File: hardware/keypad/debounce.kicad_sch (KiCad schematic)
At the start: 108 parts, among them SW401 DISPLAY, SW402 RUN, SW403 LEFT, SW404 MEMORY, SW405 COMP, SW406 UP, SW407 MENU, SW408 DOWN, SW409 INFEED, SW410 ENTER, SW411 RIGHT, SW412 DECIMAL, SW413 HEAD_POS, SW414 1, SW415 4, SW416 7, SW417 FTI, SW418 2, SW419 5, SW420 8, SW421 SHEAR, SW422 3, SW423 6, SW424 9, SW425 PAUSE, SW426 PLUS, SW427 MINUS, SW428 0, U401 SN74HC14PWR, U402 SN74HC14PWR, U403 SN74HC14PWR, U404 SN74HC14PWR, U405 SN74HC14PWR, U406 SN74LVC2G14DBV, U407 PCF8575DBR, U408 PCF8575DBR, U409 74LVC1G32GW,125

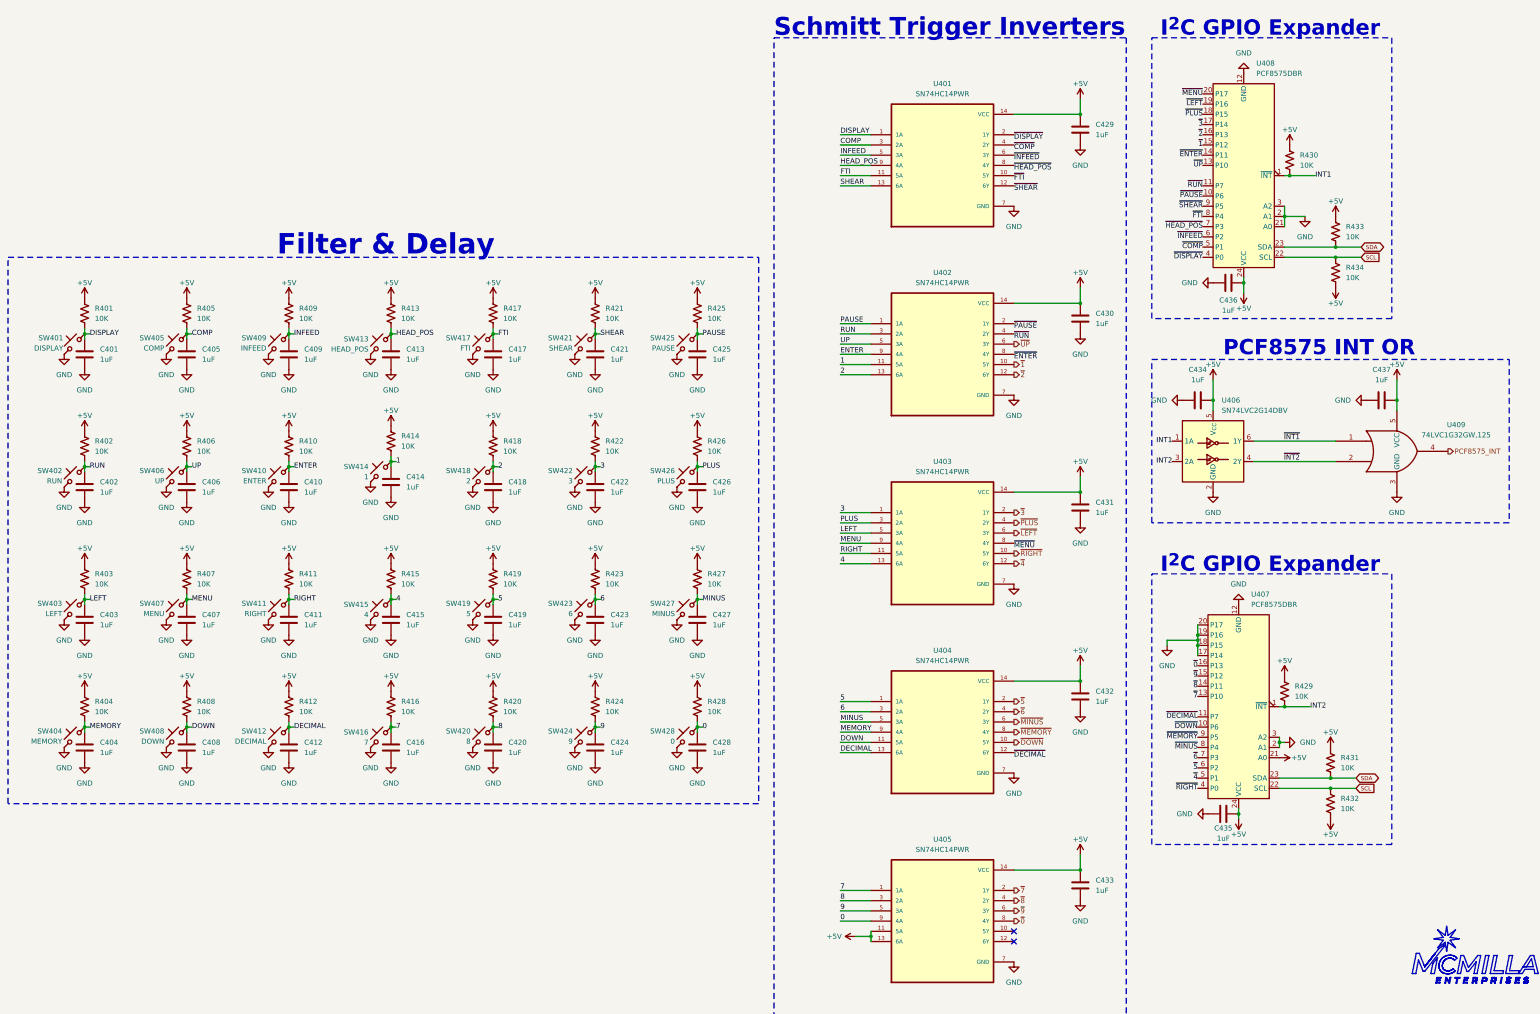
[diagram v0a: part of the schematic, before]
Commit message: [fix] repeater and sbc shutdown circuit
Fixed repeater and SBC shutdown circuit. Switched +5V VCC to +3.3V. Added C211
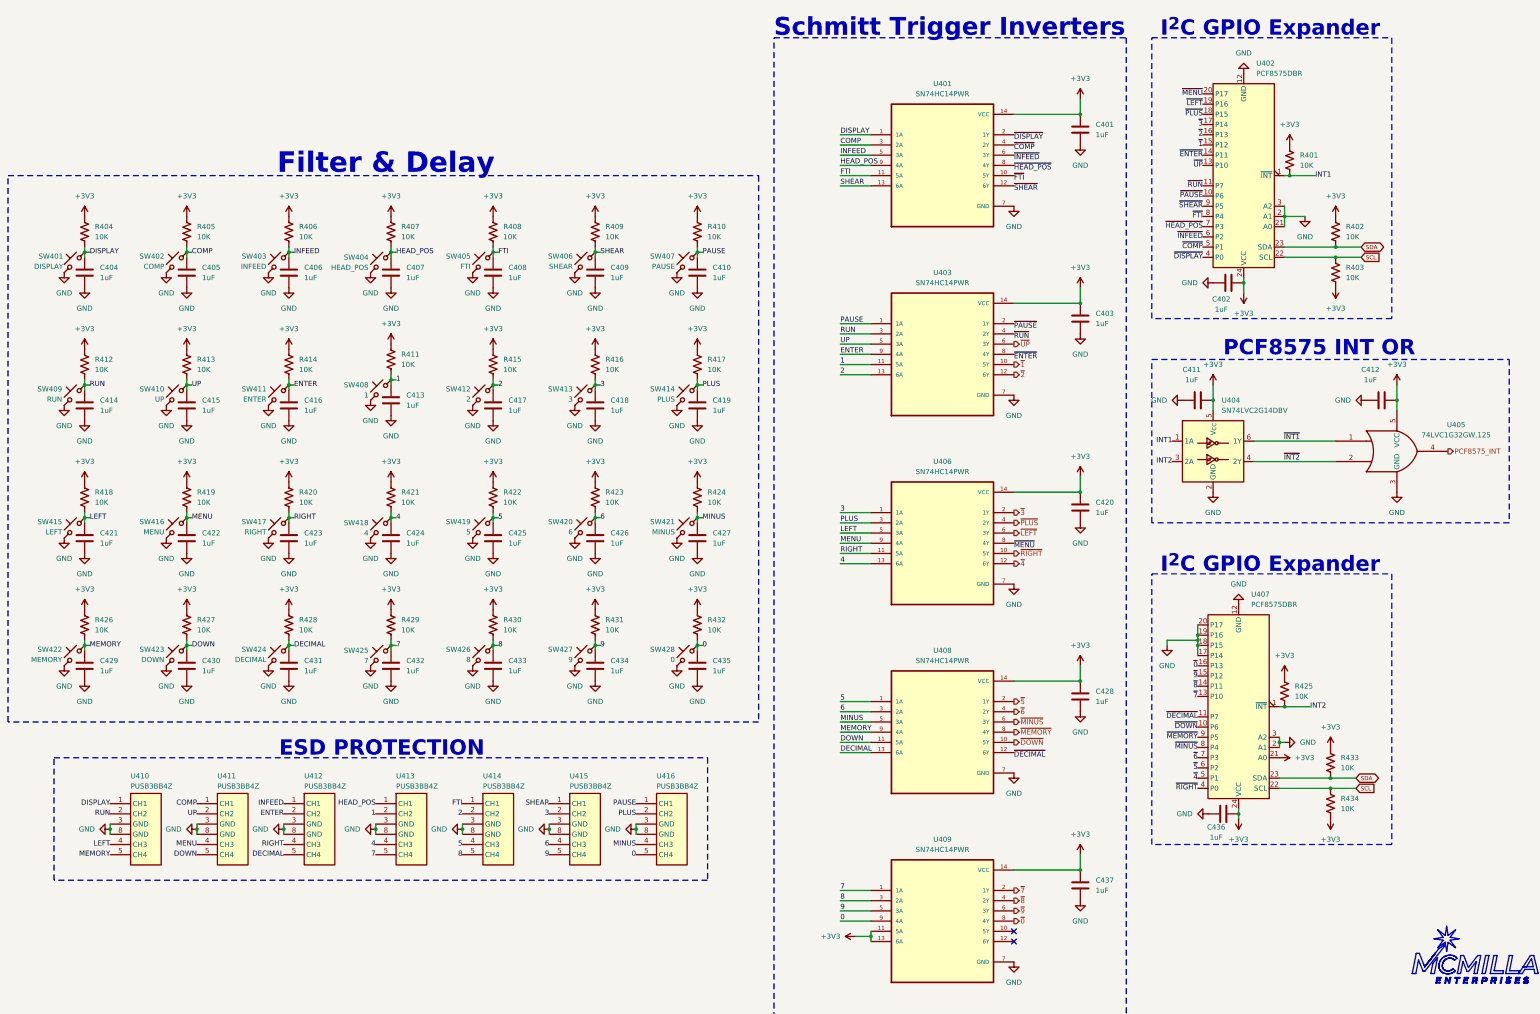
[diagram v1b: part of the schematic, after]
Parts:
- added U410, U411, U412, U413, U414, U415, U416: PUSB3BB4Z, PUSB3BB4Z:SON50P100X250X50-10N, symbol PUSB3BB4Z:PUSB3BB4Z
- renumbered C429 to C401, C436 to C402, C430 to C403, C401 to C404, C409 to C406, C413 to C407, C417 to C408, C421 to C409, C425 to C410, C434 to C411, C437 to C412, C414 to C413, C402 to C414, C406 to C415, C410 to C416, C418 to C417, C422 to C418, C426 to C419, C431 to C420, C403 to C421, C407 to C422, C411 to C423, C415 to C424, C419 to C425, C423 to C426, C432 to C428, C404 to C429, C408 to C430, C412 to C431, C416 to C432, C420 to C433, C424 to C434, C428 to C435, C435 to C436, C433 to C437, R430 to R401, R433 to R402, R434 to R403, R401 to R404, R409 to R406, R413 to R407, R417 to R408, R421 to R409, R425 to R410, R414 to R411, R402 to R412, R406 to R413, R410 to R414, R418 to R415, R422 to R416, R426 to R417, R403 to R418, R407 to R419, R411 to R420, R415 to R421, R419 to R422, R427 to R424, R429 to R425, R404 to R426, R408 to R427, R412 to R428, R416 to R429, R420 to R430, R424 to R431, R428 to R432, R431 to R433, R432 to R434, SW405 to SW402, SW409 to SW403, SW413 to SW404, SW417 to SW405, SW421 to SW406, SW425 to SW407, SW414 to SW408, SW402 to SW409, SW406 to SW410, SW410 to SW411, SW418 to SW412, SW422 to SW413, SW426 to SW414, SW403 to SW415, SW407 to SW416, SW411 to SW417, SW415 to SW418, SW423 to SW420, SW427 to SW421, SW404 to SW422, SW408 to SW423, SW412 to SW424, SW416 to SW425, SW420 to SW426, SW424 to SW427, U408 to U402, U402 to U403, U406 to U404, U409 to U405, U403 to U406, U404 to U408, U405 to U409
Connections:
- net 0: now also U416.5 (CH4)
- net 1: now also U413.2 (CH2)
- net 2: now also U414.2 (CH2)
- net 3: now also U415.2 (CH2)
- net 4: now also U413.4 (CH3)
- net 5: now also U414.4 (CH3)
- net 6: now also U415.4 (CH3)
- net 7: now also U413.5 (CH4)
- net 8: now also U414.5 (CH4)
- net 9: now also U415.5 (CH4)
- net COMP: now also U411.1 (CH1)
- net DECIMAL: now also U412.5 (CH4)
- net DISPLAY: now also U410.1 (CH1)
- net DOWN: now also U411.5 (CH4)
- net ENTER: now also U412.2 (CH2)
- net FTI: now also U414.1 (CH1)
- net GND: now also U410.3 (GND), U410.8 (GND), U411.3 (GND), U411.8 (GND), U412.3 (GND), U412.8 (GND), U413.3 (GND), U413.8 (GND), U414.3 (GND), U414.8 (GND), U415.3 (GND), U415.8 (GND), U416.3 (GND), U416.8 (GND)
- net HEAD_POS: now also U413.1 (CH1)
- net INFEED: now also U412.1 (CH1)
- net LEFT: now also U410.4 (CH3)
- net MEMORY: now also U410.5 (CH4)
- net MENU: now also U411.4 (CH3)
- net MINUS: now also U416.4 (CH3)
- net PAUSE: now also U416.1 (CH1)
- net PLUS: now also U416.2 (CH2)
- net RIGHT: now also U412.4 (CH3)
- net RUN: now also U410.2 (CH2)
- net SHEAR: now also U415.1 (CH1)
- net UP: now also U411.2 (CH2)
- net +5V renamed +3V3
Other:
- note added: "ESD PROTECTION"
- moved on the sheet: C404, C405, C406, C407, C408, C409, C410, C413, C414, C415, C416, C417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
